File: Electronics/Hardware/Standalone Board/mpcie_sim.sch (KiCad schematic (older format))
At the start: 27 parts

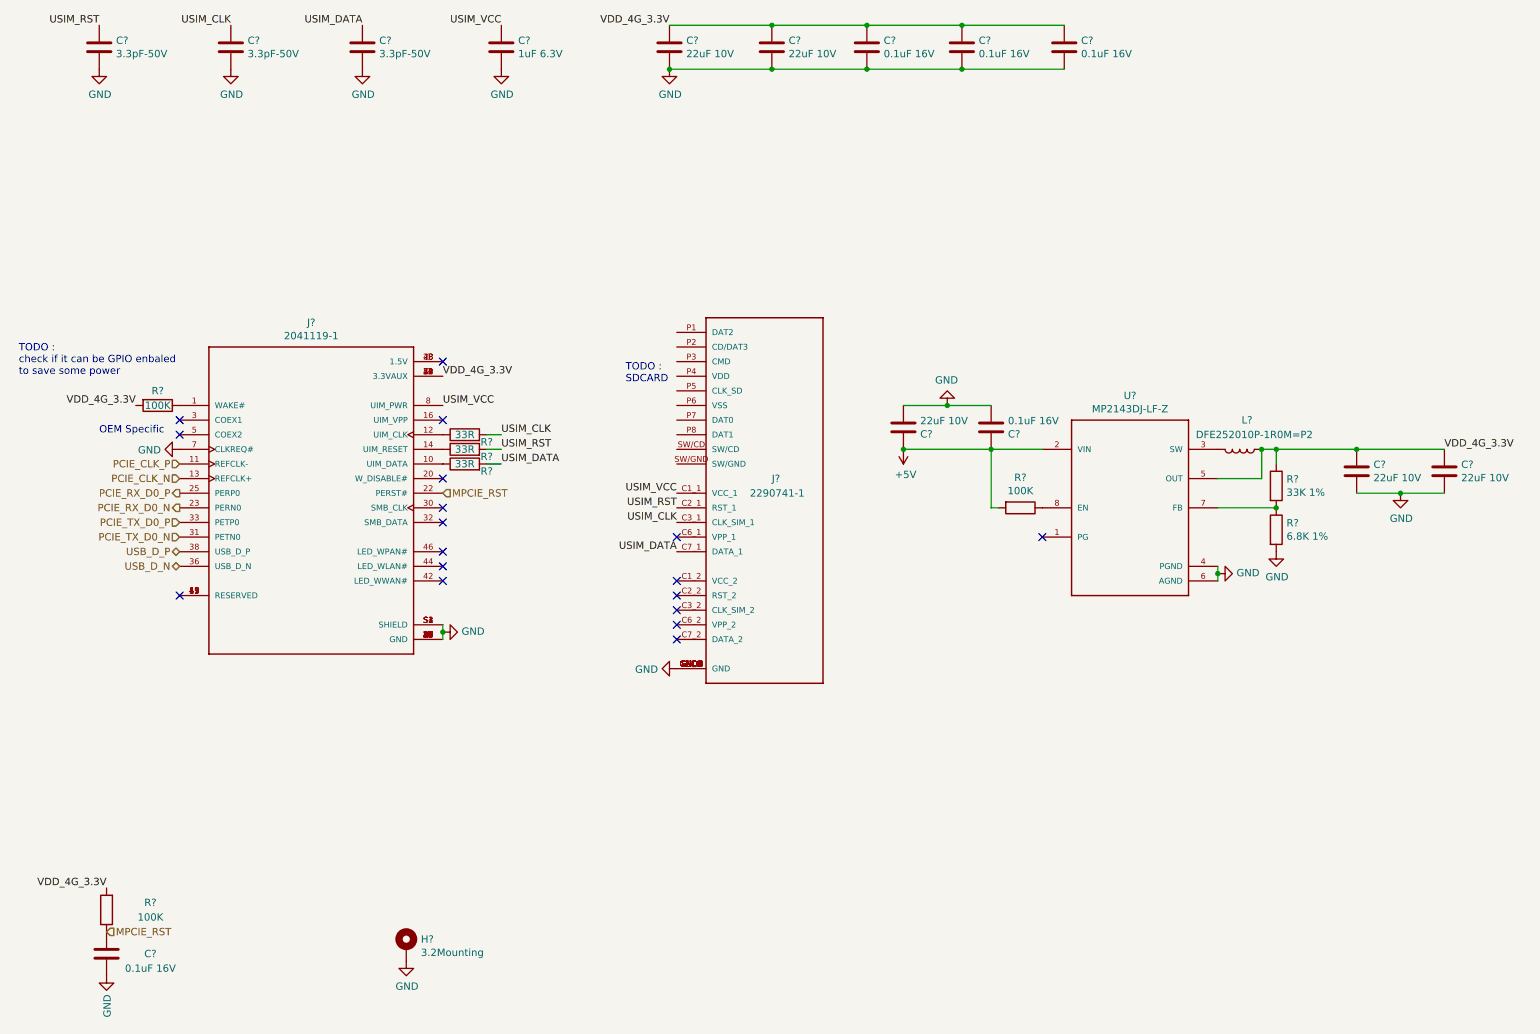
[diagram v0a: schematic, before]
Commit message: Add debug uart, gps uart, fan control and sdcard
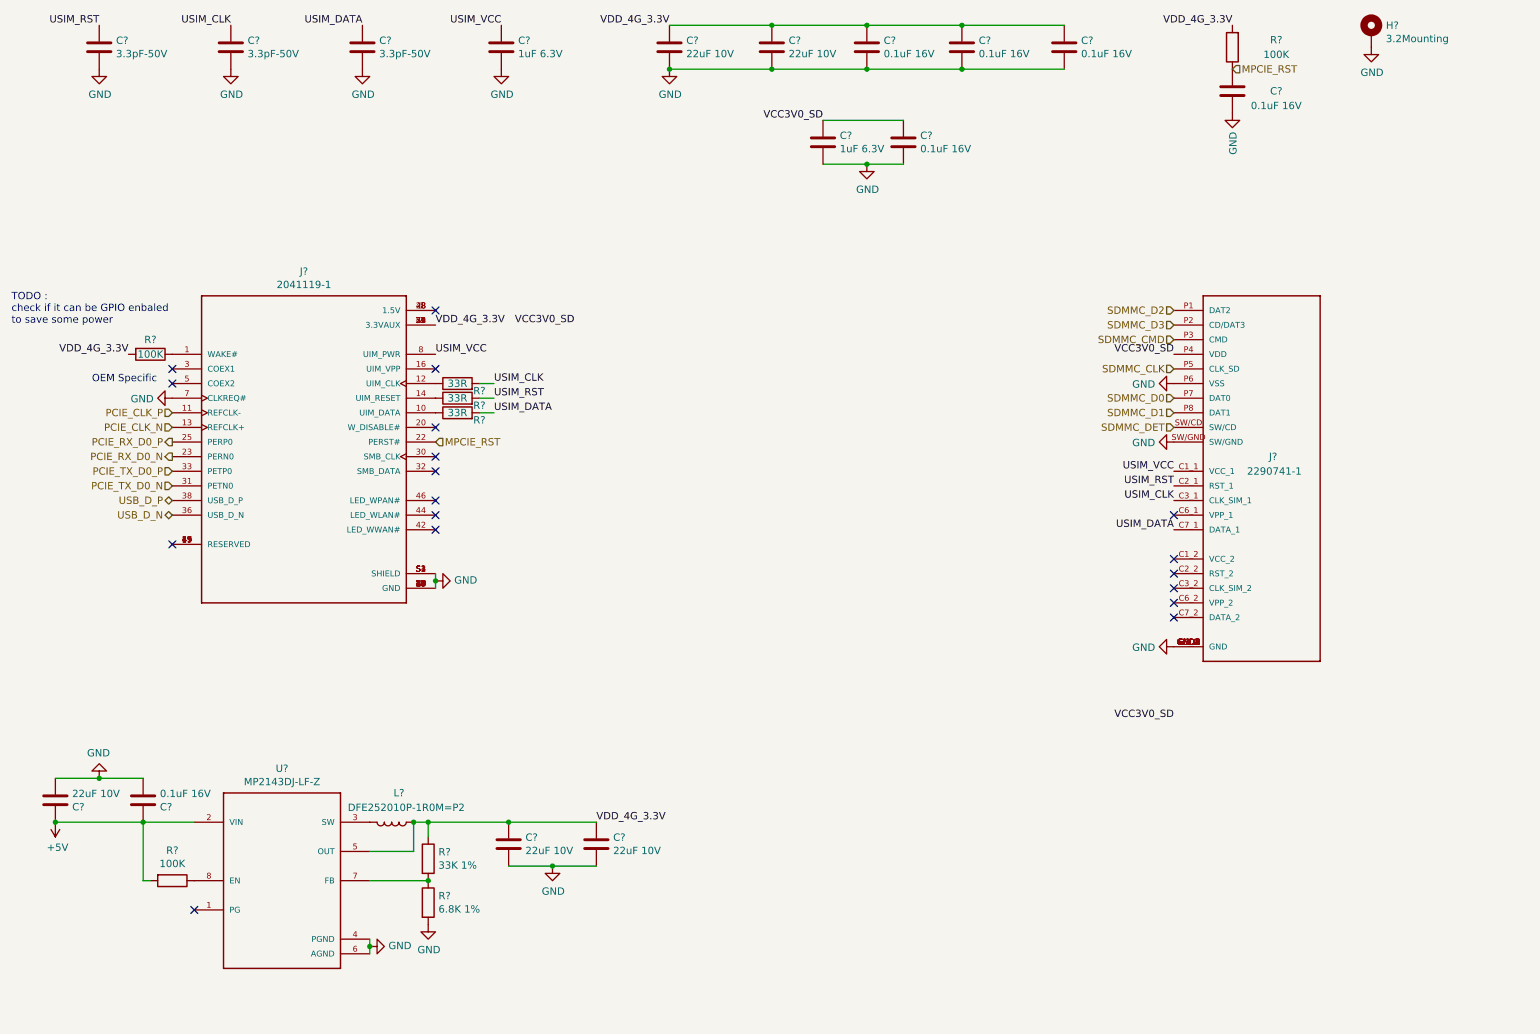
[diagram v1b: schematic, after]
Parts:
- added C?: 1uF 6.3V, symbol Device:C
- added C?: 0.1uF 16V, symbol Device:C
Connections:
- net GND: now also J?.P6 (VSS), J?.SW/GND, C?.2, C?.2
- net SDMMC_D2: now reaches J?.P1 (DAT2)
- net SDMMC_D3: now reaches J?.P2 (CD/DAT3)
- net SDMMC_CMD: now reaches J?.P3 (CMD)
- net VCC3V0_SD: now reaches J?.P4 (VDD)
- net VCC3V0_SD: now also C?.1, C?.1
- net SDMMC_CLK: now reaches J?.P5 (CLK_SD)
- net SDMMC_D0: now reaches J?.P7 (DAT0)
- net SDMMC_D1: now reaches J?.P8 (DAT1)
- net SDMMC_DET: now reaches J?.SW/CD
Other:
- note removed: "TODO :\nSDCARD"
- moved on the sheet: C?, H?, J?, L?, R?, U?

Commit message: Fix all i2c voltage, add power/reset/recovery button, Mipi dsi hig level, add 3.0/3.3/5/1.1 volt power rail
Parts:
- removed C?: 0.1uF 16V, symbol Device:C
- removed R?: 100K, symbol Device:R
- added C? (x4): 0.1uF, symbol Device:C_Small
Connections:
- net PCIE_CLK_N: now also C?.2; no longer J?.13 (REFCLK+)
- net PCIE_CLK_P: now also C?.2; no longer J?.11 (REFCLK-)
- net PCIE_TX_D0_N: now also C?.2; no longer J?.31 (PETN0)
- net PCIE_TX_D0_P: now also C?.2; no longer J?.33 (PETP0)
- net VDD_4G_3.3V: no longer R?.2
- net I2C_SDA: now reaches J?.30 (SMB_CLK)
- net I2C_SCL: now reaches J?.32 (SMB_DATA)
- net MPCIE_RST renamed PCIE_RST_N
- new net: C?.1, J?.13 (REFCLK+)
- new net: C?.1, J?.11 (REFCLK-)
- new net: C?.1, J?.33 (PETP0)
- new net: C?.1, J?.31 (PETN0)
- new net PCIE_WAKE_N: R?.2
- no-connect marks 18 -> 16
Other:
- note removed: "TODO :\ncheck if it can be GPIO enbaled\nto save some power"
- moved on the sheet: C?, H?, J?, L?, R?, U?

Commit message: Everything is routed, TODO : lenghtmatching + impedance matching + cleaning
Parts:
- removed C? (x3): 22uF 10V, symbol Device:C
- removed C?: 0.1uF 16V, symbol Device:C
- removed L?: DFE252010P-1R0M=P2, symbol Device:L
- removed R?: 100K, symbol Device:R
- removed R?: 33K 1%, symbol Device:R
- removed R?: 6.8K 1%, symbol Device:R
- removed U?: MP2143DJ-LF-Z, SOT65P280X100-8N, symbol MP2143DJ-LF-Z:MP2143DJ-LF-Z
- C10, C11, C12, C13, C14, C15, C18, C19, C2, C4, C5, C6, C7: renamed from C?; footprint (none) -> Capacitor_SMD:C_0402_1005Metric
- C3, C9: renamed from C?; footprint (none) -> Capacitor_SMD:C_0805_2012Metric
- H7: renamed from H?; footprint (none) -> MountingHole:MountingHole_3.2mm_M3_Pad
- J6: renamed from J?; footprint TE_2041119-1 -> 2041119-1:TE_2041119-1
- J7: renamed from J?; footprint TE_2290741-1 -> 2290741-1:TE_2290741-1
- R23, R27, R28, R29: renamed from R?; footprint (none) -> Resistor_SMD:R_0201_0603Metric
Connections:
- net VDD_4G_3.3V renamed +3V3
- no-connect marks 16 -> 15
